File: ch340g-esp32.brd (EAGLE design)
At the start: 36 x 20 mm, 23 parts, among them J1 USB4105_REVA, Q1 12MHz, T1 BC847, T2 BC847, U1 CH340G

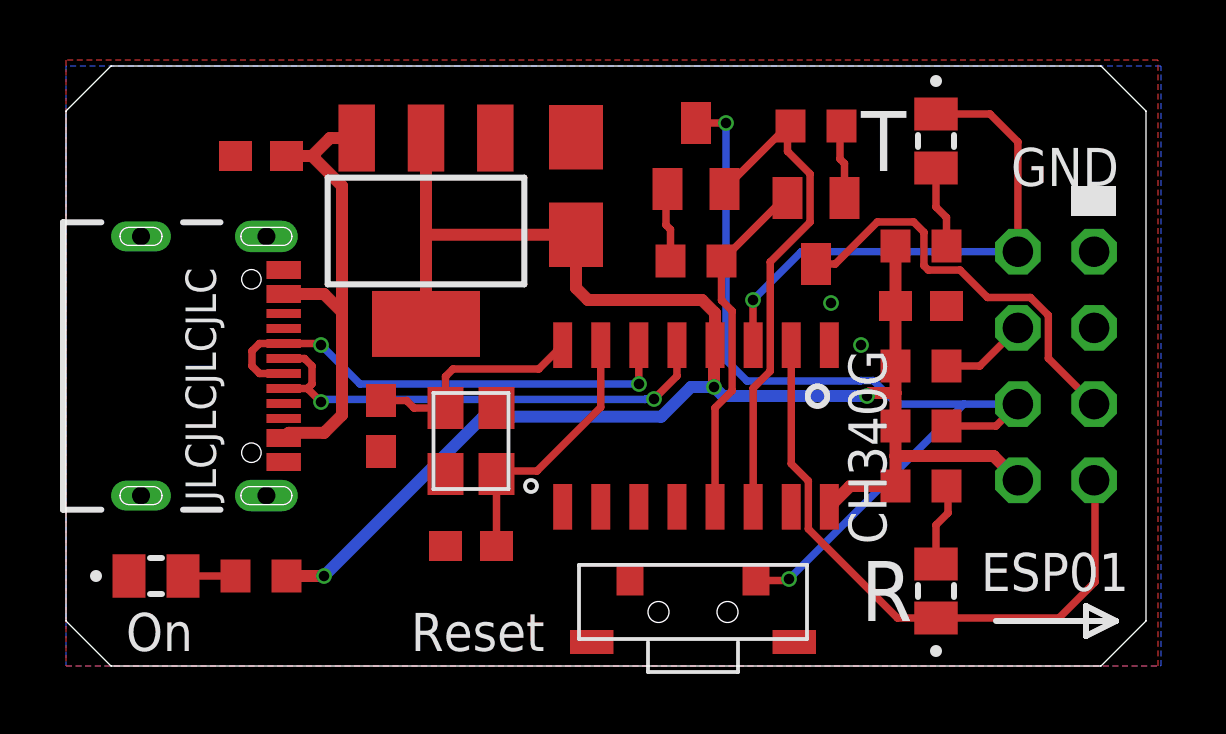
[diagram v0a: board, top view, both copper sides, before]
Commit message: Added support for powering from USB Cable
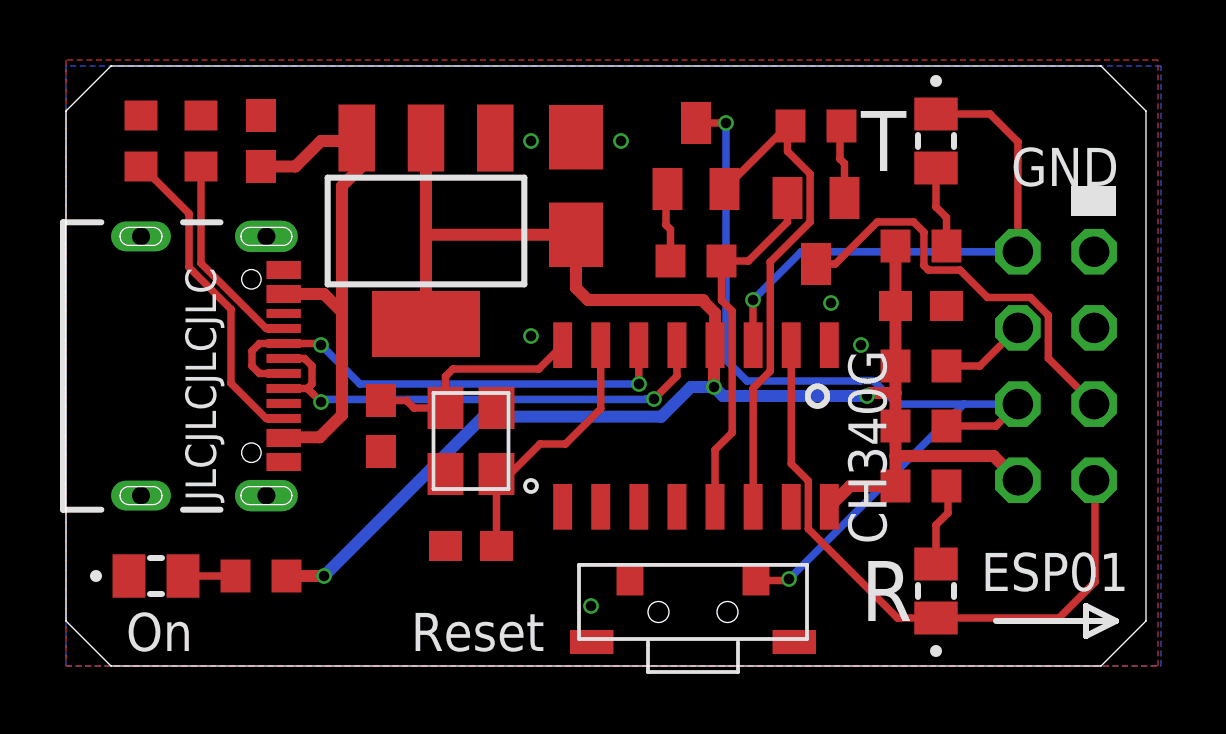
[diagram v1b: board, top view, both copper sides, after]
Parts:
- added R8, R9: 5.1K, rcl:R0603
- moved C3 0.50 mm to (6.50, 17.5), turned to 90 degrees
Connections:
- new net N$7: J1.A5, R8.2
- new net N$8: J1.B5, R9.1
- net GND: now also R8.1, R9.2
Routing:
- net N$8: track 0.00 -> 10.7 mm
- net N$7: track 0.00 -> 6.88 mm
- net +3V3: track 58.4 -> 62.2 mm
- net VBUS: track 16.1 -> 17.6 mm
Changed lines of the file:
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@@
 <setting verticaltext="up"/>
 </settings>
-<grid distance="0.5" unitdist="mm" unit="mm" style="lines" multiple="1" display="yes" altdistance="0.1" altunitdist="mm" altunit="mm"/>
+<grid distance="0.5" unitdist="mm" unit="mm" style="lines" multiple="1" display="yes" altdistance="0.05" altunitdist="mm" altunit="mm"/>
 <layers>
 <layer number="1" name="Top" color="4" fill="1" visible="yes" active="yes"/>
@@
 <attribute name="PRICE" value="None" x="29" y="2.5" size="1.778" layer="27" rot="R90" display="off"/>
 </element>
-<element name="C3" library="rcl" library_urn="urn:adsk.eagle:library:334" package="C0603" package3d_urn="urn:adsk.eagle:package:23616/2" value="10u" x="6.5" y="17" smashed="yes" rot="R180">
-<attribute name="POPULARITY" value="73" x="6.5" y="17" size="1.778" layer="27" rot="R180" display="off"/>
-<attribute name="SPICEPREFIX" value="C" x="6.5" y="17" size="1.778" layer="27" rot="R180" display="off"/>
+<element name="C3" library="rcl" library_urn="urn:adsk.eagle:library:334" package="C0603" package3d_urn="urn:adsk.eagle:package:23616/2" value="10u" x="6.5" y="17.5" smashed="yes" rot="R90">
+<attribute name="POPULARITY" value="73" x="6.5" y="17.5" size="1.778" layer="27" rot="R90" display="off"/>
+<attribute name="SPICEPREFIX" value="C" x="6.5" y="17.5" size="1.778" layer="27" rot="R90" display="off"/>
 </element>
 <element name="C4" library="rcl" library_urn="urn:adsk.eagle:library:334" package="B/3528-21W" package3d_urn="urn:adsk.eagle:package:23411/1" value="100u" x="17" y="16" smashed="yes" rot="R270">
@@
 <attribute name="MF" value="SHOU HAN" x="20.9" y="1.8" size="1.778" layer="27" display="off"/>
 <attribute name="MP" value="TS36CA-0.7" x="20.9" y="1.8" size="1.778" layer="27" display="off"/>
+</element>
+<element name="R8" library="rcl" library_urn="urn:adsk.eagle:library:334" package="R0603" package3d_urn="urn:adsk.eagle:package:23555/3" value="5.1K" x="4.5" y="17.5" smashed="yes" rot="R270">
+<attribute name="POPULARITY" value="70" x="4.5" y="17.5" size="1.778" layer="27" rot="R270" display="off"/>
+<attribute name="SPICEPREFIX" value="R" x="4.5" y="17.5" size="1.778" layer="27" rot="R270" display="off"/>
+</element>
+<element name="R9" library="rcl" library_urn="urn:adsk.eagle:library:334" package="R0603" package3d_urn="urn:adsk.eagle:package:23555/3" value="5.1K" x="2.5" y="17.5" smashed="yes" rot="R90">
+<attribute name="POPULARITY" value="70" x="2.5" y="17.5" size="1.778" layer="27" rot="R90" display="off"/>
+<attribute name="SPICEPREFIX" value="R" x="2.5" y="17.5" size="1.778" layer="27" rot="R90" display="off"/>
 </element>
 </elements>
@@
 <via x="26.5" y="10.7" extent="1-16" drill="0.35"/>
 <via x="25.5" y="12.1" extent="1-16" drill="0.35"/>
+<contactref element="R8" pad="1"/>
+<contactref element="R9" pad="2"/>
+<via x="15.5" y="11" extent="1-16" drill="0.35"/>
+<via x="15.5" y="17.5" extent="1-16" drill="0.35"/>
+<via x="18.5" y="17.5" extent="1-16" drill="0.35"/>
+<via x="17.5" y="2" extent="1-16" drill="0.35"/>
 </signal>
 <signal name="VBUS" class="2">
@@
 <contactref element="J1" pad="A4/B9"/>
 <contactref element="C3" pad="1"/>
-<wire x1="7.35" y1="17" x2="8.2" y2="17" width="0.4" layer="1"/>
-<wire x1="8.799" y1="17.599" x2="9.689" y2="17.599" width="0.4" layer="1"/>
-<wire x1="8.2" y1="17" x2="8.799" y2="17.599" width="0.4" layer="1"/>
-<wire x1="7.255" y1="7.6" x2="7.428" y2="7.773" width="0.4" layer="1"/>
-<wire x1="7.428" y1="7.773" x2="8.60668125" y2="7.773" width="0.4" layer="1"/>
-<wire x1="8.60668125" y1="7.773" x2="9.2" y2="8.36631875" width="0.4" layer="1"/>
+<wire x1="8.45668125" y1="7.623" x2="7.278" y2="7.623" width="0.4" layer="1"/>
+<wire x1="7.255" y1="7.6" x2="7.278" y2="7.623" width="0.4" layer="1"/>
+<wire x1="8.45668125" y1="7.623" x2="9.2" y2="8.36631875" width="0.4" layer="1"/>
 <wire x1="9.2" y1="8.36631875" x2="9.2" y2="11.8" width="0.4" layer="1"/>
 <wire x1="9.2" y1="11.8" x2="8.6" y2="12.4" width="0.4" layer="1"/>
 <wire x1="8.6" y1="12.4" x2="7.255" y2="12.4" width="0.4" layer="1"/>
-<wire x1="8.2" y1="17" x2="9.2" y2="16" width="0.4" layer="1"/>
-<wire x1="9.2" y1="16" x2="9.2" y2="11.8" width="0.4" layer="1"/>
+<wire x1="9.2" y1="11.8" x2="9.2" y2="16" width="0.4" layer="1"/>
+<wire x1="9.2" y1="16" x2="9.8" y2="16.6" width="0.4" layer="1"/>
+<wire x1="9.8" y1="16.6" x2="9.8" y2="17.488" width="0.4" layer="1"/>
+<wire x1="9.788" y1="17.5" x2="9.689" y2="17.599" width="0.4" layer="1"/>
+<wire x1="6.5" y1="16.65" x2="7.65" y2="16.65" width="0.4" layer="1"/>
+<wire x1="7.65" y1="16.65" x2="8.5" y2="17.5" width="0.4" layer="1"/>
+<wire x1="8.5" y1="17.5" x2="9.788" y2="17.5" width="0.4" layer="1"/>
+<wire x1="9.788" y1="17.5" x2="9.8" y2="17.488" width="0.4" layer="1"/>
 </signal>
 <signal name="D-">
@@
 <contactref element="Q1" pad="P$1"/>
 <wire x1="14.35" y1="6.4" x2="14.35" y2="4" width="0.25" layer="1"/>
-<wire x1="14.35" y1="6.4" x2="14.45" y2="6.5" width="0.25" layer="1"/>
-<wire x1="17.825" y1="8.625" x2="17.825" y2="10.695" width="0.25" layer="1"/>
-<wire x1="14.45" y1="6.5" x2="15.7" y2="6.5" width="0.25" layer="1"/>
-<wire x1="15.7" y1="6.5" x2="17.825" y2="8.625" width="0.25" layer="1"/>
+<wire x1="14.35" y1="6.4" x2="14.8" y2="6.4" width="0.25" layer="1"/>
+<wire x1="15.8" y1="7.4" x2="14.8" y2="6.4" width="0.25" layer="1"/>
+<wire x1="17.825" y1="8.575" x2="17.825" y2="10.695" width="0.25" layer="1"/>
+<wire x1="15.8" y1="7.4" x2="16.65" y2="7.4" width="0.25" layer="1"/>
+<wire x1="16.65" y1="7.4" x2="17.825" y2="8.575" width="0.25" layer="1"/>
 </signal>
 <signal name="RX">
@@
 <contactref element="R1" pad="1"/>
 <contactref element="T2" pad="2"/>
-<wire x1="21.85" y1="13.5" x2="23.95" y2="15.6" width="0.25" layer="1"/>
-<wire x1="23.95" y1="15.6" x2="24.05" y2="15.6" width="0.25" layer="1"/>
-<wire x1="21.635" y1="5.305" x2="21.635" y2="8.60738125" width="0.25" layer="1"/>
+<wire x1="24.05" y1="15.6" x2="24.05" y2="14.8" width="0.25" layer="1"/>
+<wire x1="21.85" y1="13.5" x2="22.75" y2="13.5" width="0.25" layer="1"/>
+<wire x1="24.05" y1="14.8" x2="22.75" y2="13.5" width="0.25" layer="1"/>
+<wire x1="21.635" y1="5.305" x2="21.635" y2="7.20738125" width="0.25" layer="1"/>
 <wire x1="21.85" y1="12.189225" x2="21.85" y2="13.5" width="0.25" layer="1"/>
-<wire x1="21.635" y1="8.60738125" x2="22.2045" y2="9.17688125" width="0.25" layer="1"/>
-<wire x1="22.2045" y1="9.17688125" x2="22.2045" y2="11.834725" width="0.25" layer="1"/>
+<wire x1="21.635" y1="7.20738125" x2="22.2045" y2="7.77688125" width="0.25" layer="1"/>
+<wire x1="22.2045" y1="7.77688125" x2="22.2045" y2="11.834725" width="0.25" layer="1"/>
 <wire x1="22.2045" y1="11.834725" x2="21.85" y2="12.189225" width="0.25" layer="1"/>
 </signal>
@@
 <wire x1="17.4" y1="12.2" x2="17" y2="12.6" width="0.4" layer="1"/>
 <wire x1="17" y1="12.6" x2="17" y2="14.375" width="0.4" layer="1"/>
-<wire x1="21.2" y1="12.2" x2="17.4" y2="12.2" width="0.4" layer="1"/>
+<wire x1="21.2" y1="12.2" x2="17.45" y2="12.2" width="0.4" layer="1"/>
+<wire x1="17.45" y1="12.2" x2="17.4" y2="12.2" width="0.4" layer="1"/>
 <wire x1="17" y1="14.375" x2="12.025" y2="14.375" width="0.4" layer="1"/>
 <wire x1="12.025" y1="14.375" x2="12" y2="14.4" width="0.4" layer="1"/>
@@
 <wire x1="26.7" y1="9" x2="21.9" y2="9" width="0.4" layer="16"/>
 <wire x1="21.9" y1="9" x2="21.6" y2="9.3" width="0.4" layer="16"/>
+<wire x1="21.25" y1="12.2" x2="17.45" y2="12.2" width="0.4" layer="1"/>
 </signal>
 <signal name="RST">
@@
 <wire x1="28.598" y1="14.45838125" x2="28.598" y2="13.34561875" width="0.25" layer="1"/>
 </signal>
+<signal name="N$7">
+<contactref element="R8" pad="2"/>
+<contactref element="J1" pad="A5"/>
+<wire x1="7.255" y1="11.25" x2="7.253" y2="11.248" width="0.25" layer="1"/>
+<wire x1="7.253" y1="11.248" x2="6.67561875" y2="11.248" width="0.25" layer="1"/>
+<wire x1="6.67561875" y1="11.248" x2="4.5" y2="13.42361875" width="0.25" layer="1"/>
+<wire x1="4.5" y1="13.42361875" x2="4.5" y2="16.65" width="0.25" layer="1"/>
+</signal>
+<signal name="N$8">
+<contactref element="J1" pad="B5"/>
+<contactref element="R9" pad="1"/>
+<wire x1="7.255" y1="8.25" x2="7.253" y2="8.248" width="0.25" layer="1"/>
+<wire x1="7.253" y1="8.248" x2="6.67561875" y2="8.248" width="0.25" layer="1"/>
+<wire x1="6.67561875" y1="8.248" x2="5.5" y2="9.42361875" width="0.25" layer="1"/>
+<wire x1="5.5" y1="9.42361875" x2="5.5" y2="11.89045625" width="0.25" layer="1"/>
+<wire x1="4.102" y1="15.08149375" x2="2.53349375" y2="16.65" width="0.25" layer="1"/>
+<wire x1="2.53349375" y1="16.65" x2="2.5" y2="16.65" width="0.25" layer="1"/>
+<wire x1="4.102" y1="13.28845625" x2="4.102" y2="15.08149375" width="0.25" layer="1"/>
+<wire x1="5.5" y1="11.89045625" x2="4.102" y2="13.28845625" width="0.25" layer="1"/>
+</signal>
 </signals>
